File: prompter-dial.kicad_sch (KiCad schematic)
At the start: 4 parts, among them SW1 JUMP_B, SW2 RUN, SW3 JUMP_F, U1 ATtiny85-20S

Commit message: Create schematic
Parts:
- added C1, C2: 0.01uF, symbol Device:C
- added R1, R2, R3, R4, R5, R6, R7, R8: 10K, symbol Device:R
- added SW4: RotaryEncoder, symbol Device:RotaryEncoder
- added SW5: RESET, Button_Switch_Keyboard:SW_Cherry_MX_1.00u_PCB, symbol Switch:SW_Push
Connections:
- net JUMP_F: now reaches SW3.1
- net JUMP_F: now also U1.7 (PB2), R3.1
- net +5V: now reaches SW3.2
- net +5V: now also SW1.2, SW2.2, U1.8 (VCC), R6.1, R7.1, SW5.2
- net JUMP_B: now reaches SW1.1
- net JUMP_B: now also U1.3 (XTAL2/PB4), R1.1
- net RUN: now reaches SW2.1
- net RUN: now also U1.2 (XTAL1/PB3), R2.1
- net RESET: now reaches U1.1 (~{RESET}/PB5)
- net RESET: now also R8.1, SW5.1
- net GND: now reaches U1.4 (GND)
- net GND: now also C1.2, C2.2, R1.2, R2.2, R3.2, R8.2, SW4.C
- net ENC_A: now reaches U1.5 (AREF/PB0)
- net ENC_A: now also R5.1
- net ENC_B: now reaches U1.6 (PB1)
- net ENC_B: now also R4.1
- new net: C1.1, R5.2, R7.2, SW4.A
- new net: C2.1, R4.2, R6.2, SW4.B
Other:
- moved on the sheet: SW3, U1

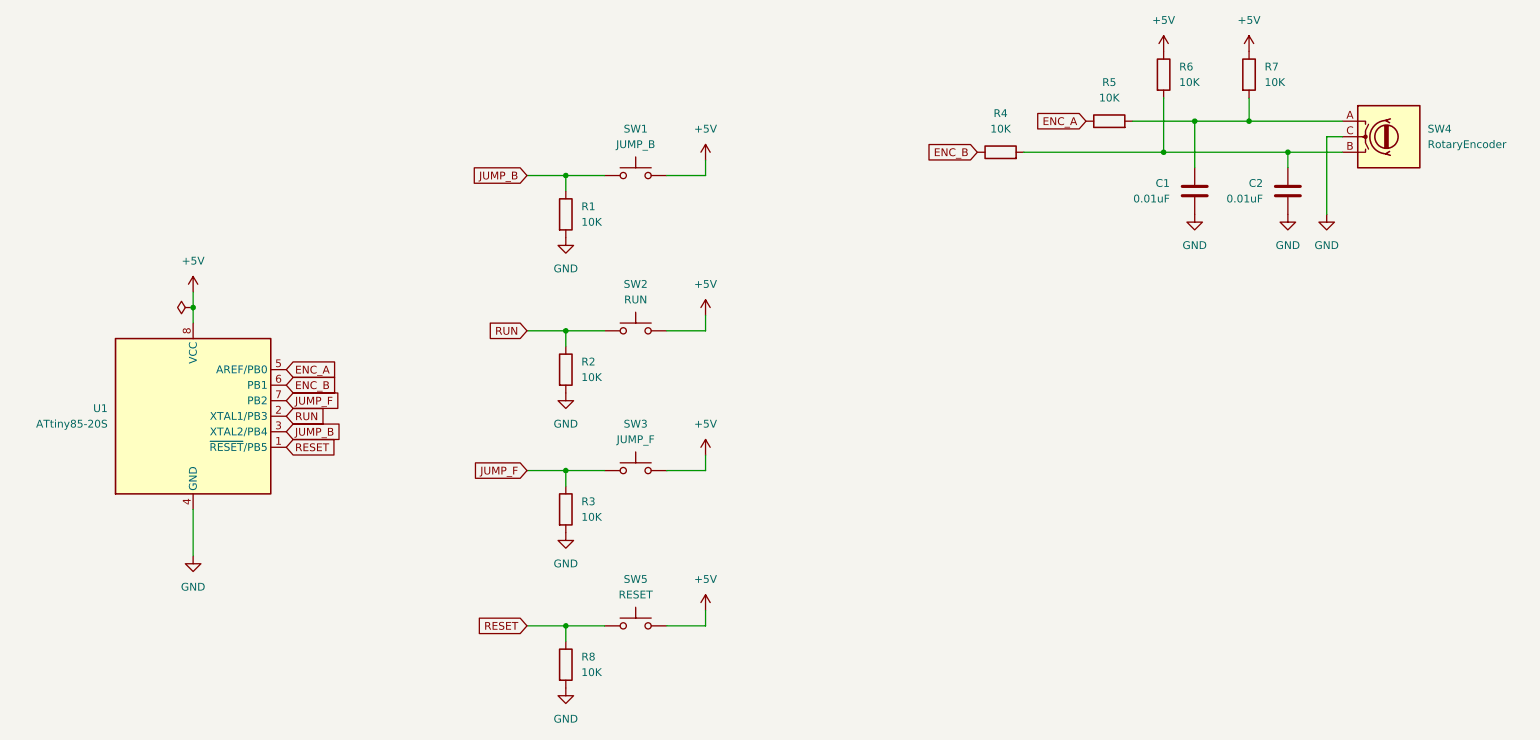
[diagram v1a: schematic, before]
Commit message: Remove caps
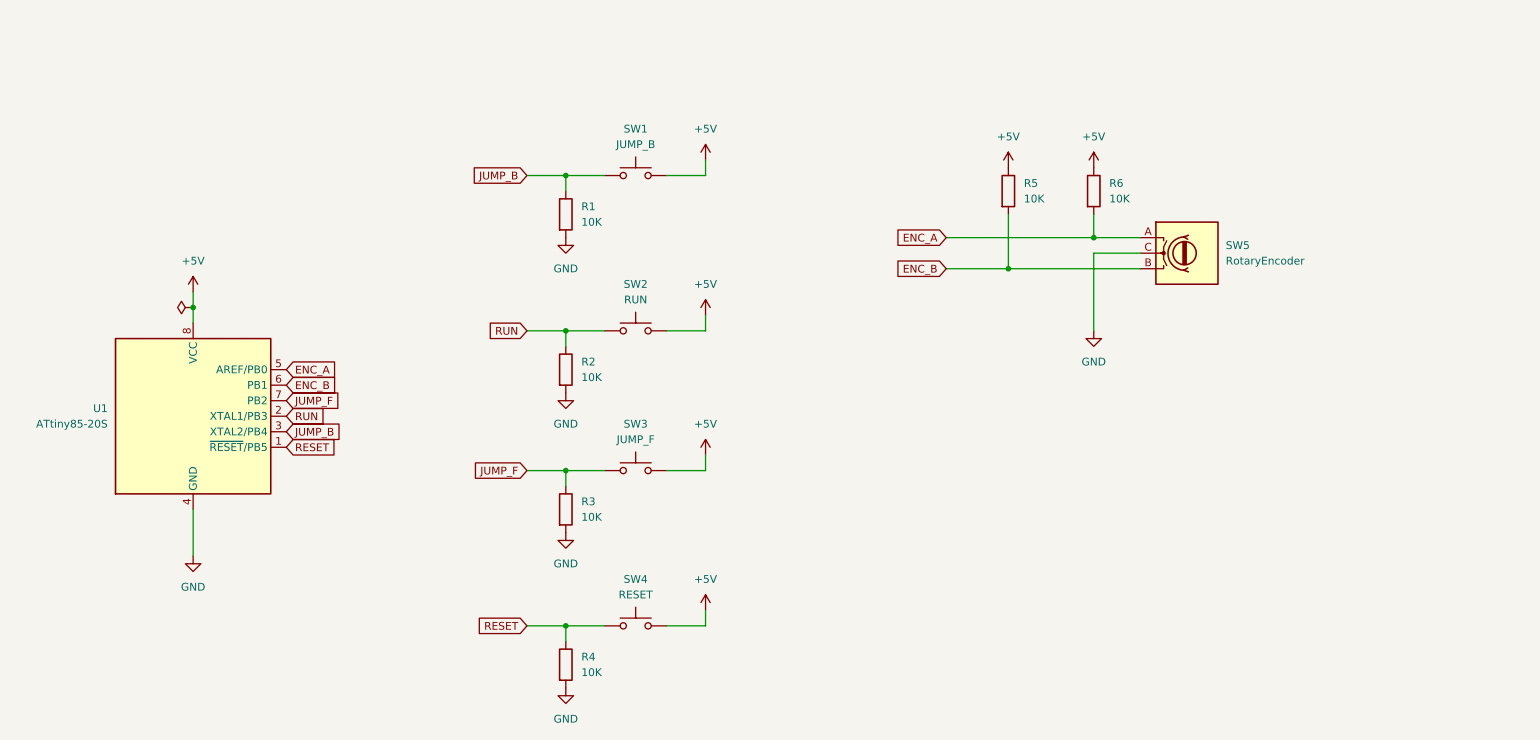
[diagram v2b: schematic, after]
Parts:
- removed C1, C2: 0.01uF, symbol Device:C
- removed R4, R5: 10K, symbol Device:R
- renumbered R8 to R4, R6 to R5, R7 to R6, SW5 to SW4, SW4 to SW5
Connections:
- net ENC_A: now also R6.2, SW5.A
- net ENC_B: now also R5.2, SW5.B
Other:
- moved on the sheet: R5, R6, SW5

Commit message: Reduce to match available pins
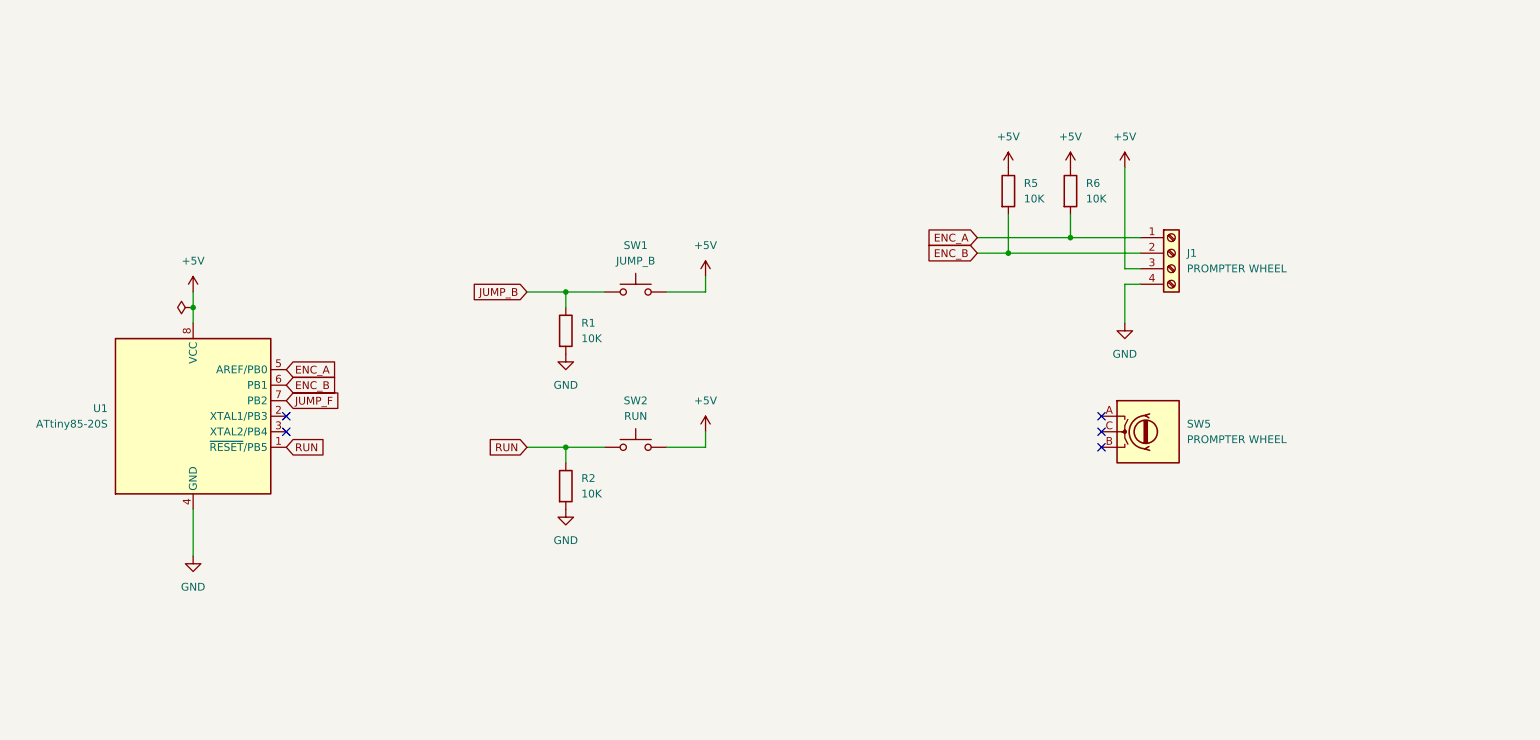
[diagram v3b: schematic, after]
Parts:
- removed R3, R4: 10K, symbol Device:R
- removed SW3: JUMP_F, Button_Switch_Keyboard:SW_Cherry_MX_1.00u_PCB, symbol Switch:SW_Push
- removed SW4: RESET, Button_Switch_Keyboard:SW_Cherry_MX_1.00u_PCB, symbol Switch:SW_Push
- added J1: PROMPTER WHEEL, Connector_JST:JST_XH_B4B-XH-A_1x04_P2.50mm_Vertical, symbol Connector:Screw_Terminal_01x04
- R1, R2, R5, R6: footprint (none) -> Resistor_THT:R_Axial_DIN0204_L3.6mm_D1.6mm_P5.08mm_Horizontal
- SW5: value RotaryEncoder -> PROMPTER WHEEL
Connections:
- net RESET is gone; now on net RUN: U1.1 (~{RESET}/PB5)
- net +5V: now also J1.3 (Pin_3)
- net ENC_A: now also J1.1 (Pin_1); no longer SW5.A
- net ENC_B: now also J1.2 (Pin_2); no longer SW5.B
- net GND: now also J1.4 (Pin_4); no longer SW5.C
- net JUMP_B: no longer U1.3 (XTAL2/PB4)
- net RUN: no longer U1.2 (XTAL1/PB3)
- no-connect marks 0 -> 5
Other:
- moved on the sheet: R1, R2, R6, SW1, SW2

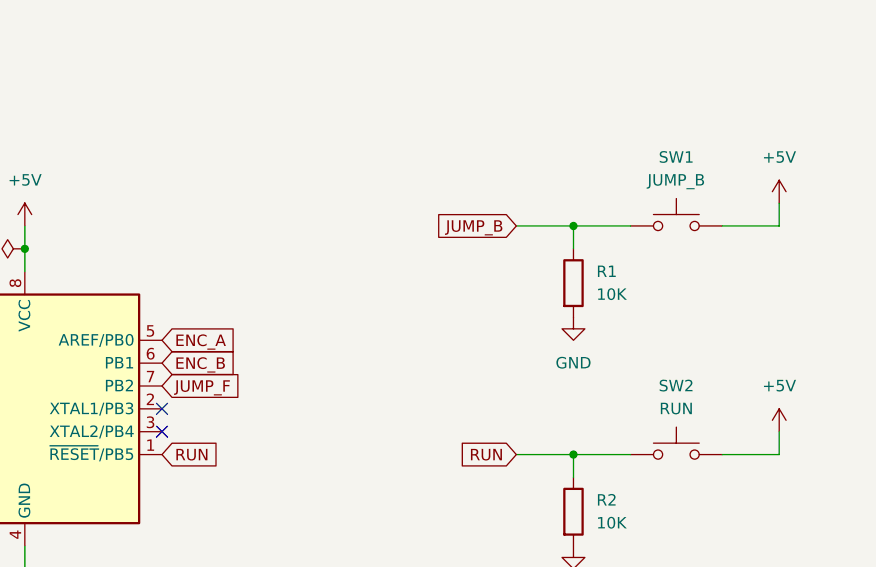
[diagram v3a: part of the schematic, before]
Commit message: Add drill hole
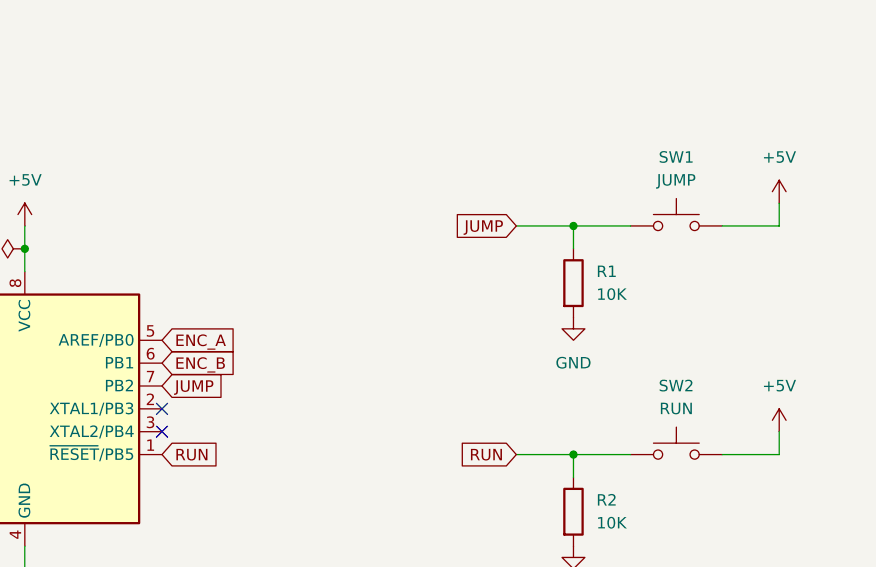
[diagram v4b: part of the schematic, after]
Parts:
- SW1: value JUMP_B -> JUMP
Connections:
- net JUMP_F is gone; now on net JUMP: U1.7 (PB2)
- net JUMP_B renamed JUMP
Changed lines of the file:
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@@
 		)
 	)
-	(global_label "JUMP_F"
+	(global_label "JUMP"
 		(shape input)
 		(at 73.66 87.63 0)
@@
 		)
 		(property "Intersheetrefs" "${INTERSHEET_REFS}"
-			(at 83.7209 87.63 0)
+			(at 81.6647 87.63 0)
 			(hide yes)
 			(show_name no)
@@
 		)
 	)
-	(global_label "JUMP_B"
+	(global_label "JUMP"
 		(shape input)
 		(at 113.03 69.85 180)
@@
 		)
 		(property "Intersheetrefs" "${INTERSHEET_REFS}"
-			(at 102.7877 69.85 0)
+			(at 105.0253 69.85 0)
 			(hide yes)
 			(show_name no)
@@
 			)
 		)
-		(property "Value" "JUMP_B"
+		(property "Value" "JUMP"
 			(at 130.81 64.77 0)
 			(show_name no)
